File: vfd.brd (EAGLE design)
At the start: 41 parts, among them J1 KEYPAD, J3 ARDUINO_R3, U1 20070-1A04PTH, X1 DRV

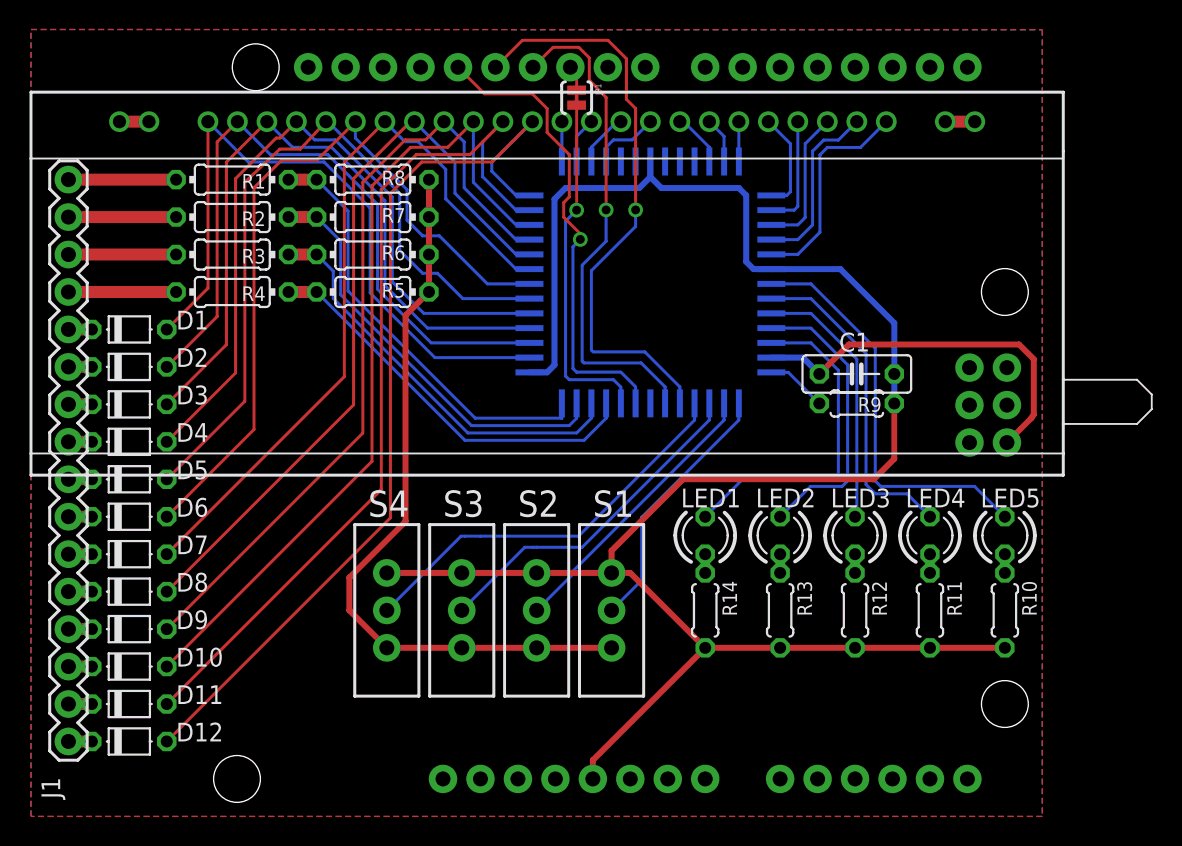
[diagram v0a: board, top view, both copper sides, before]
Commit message: add filament driver components
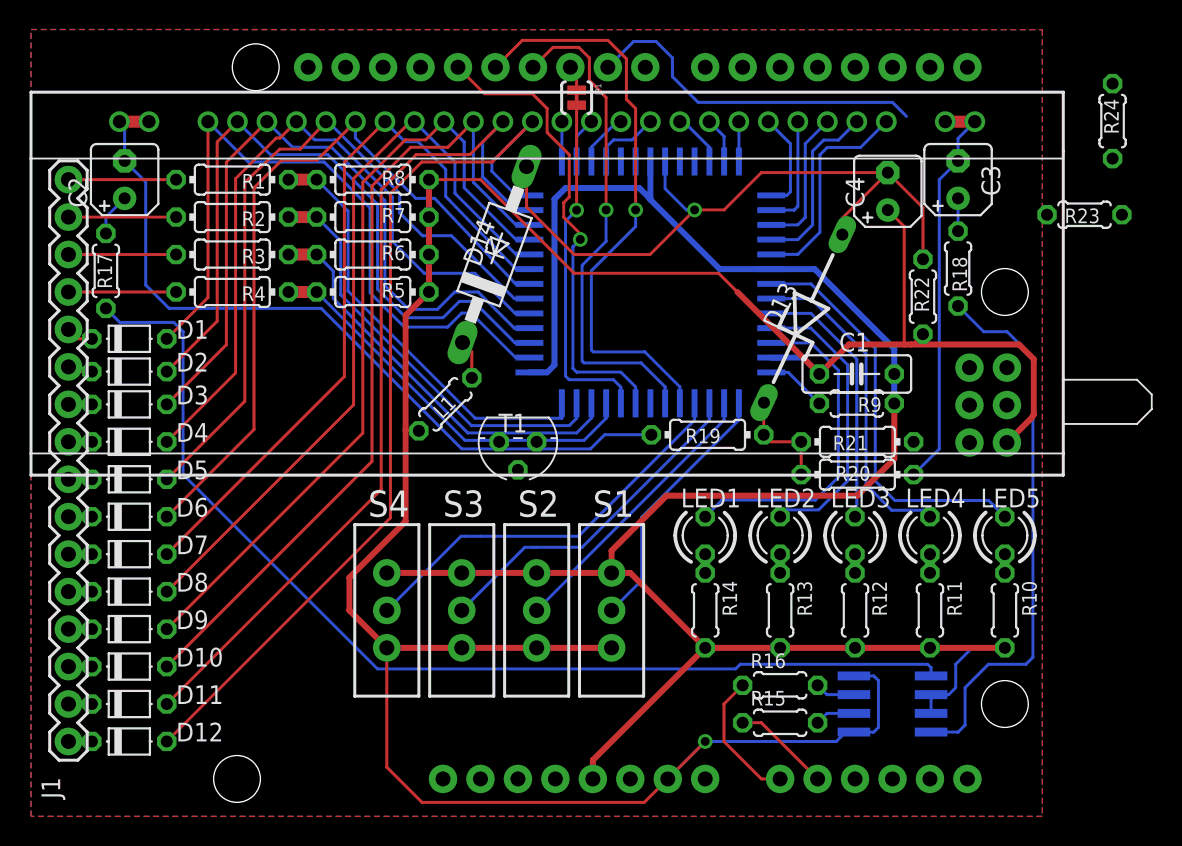
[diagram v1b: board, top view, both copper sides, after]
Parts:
- added C2, C3: 4u7, resistor:B45181A
- added C4: 22uf/50v, resistor:B45181A
- added D13: (no value), diode:ZDIO12.5
- added D14: SS14, diode:F126Z12
- added L1: 1MH, resistor:0204/5
- added R15, R16: 20K, resistor:0204/5
- added R17, R18: 1R0, resistor:0204/5
- added R19, R20: 3k0, resistor:0204/7
- added R21: 100k, resistor:0204/7
- added R22: 100k, resistor:0204/5
- added R23: 10k, resistor:0204/5
- added R24: 1k5, resistor:0204/5
- added T1: 8550, transistor:TO92
- added U$1: L9110, Drivers:SOP8-1.27-5X3.6MM
- moved D1 0.64 mm to (6.67, 32.4)
- moved D2 0.32 mm to (6.67, 30.2)
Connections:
- removed net N$14: X1.P$34
- removed net N$19: J3.AREF
- new net DRVF1: J3.A1, R15.1
- new net DRVF2: J3.A0, R16.1
- new net HVDRV: J3.D9, R24.2
- new net N$26: R15.2, U$1.6
- new net N$27: R16.2, U$1.7
- new net N$28: R17.1, U$1.1
- new net N$29: R18.1, U$1.4
- new net N$30: C2.+, R17.2
- new net N$31: C3.+, R18.2
- new net N$35: D13.C, R19.1, R20.2, R21.2
- new net N$36: R23.1, R24.1, T1.2
- new net N$40: D14.C, L1.1, T1.3
- new net VEE: C4.-, D13.A, D14.A, R22.2, X1.P$34
- net FIL1: now also C2.-, R19.2
- net FIL2: now also C3.-, R20.1
- net GND: now also C4.+, L1.2, R21.1, R22.1, U$1.5, U$1.8
- net VCC: now also R23.2, T1.1, U$1.2, U$1.3
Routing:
- net GND: track 76.2 -> 172.8 mm, vias 0 -> 1
- net N$28: track 0.00 -> 72.5 mm
- net FIL1: track 2.00 -> 53.1 mm
- net VEE: track 0.00 -> 47.7 mm, vias 0 -> 1
- net N$29: track 0.00 -> 37.3 mm
- net FIL2: track 2.00 -> 27.7 mm
- net HVDRV: track 0.00 -> 23.8 mm
- net DRVF2: track 0.00 -> 9.20 mm
- net N$35: track 0.00 -> 7.15 mm
- net DRVF1: track 0.00 -> 6.66 mm
- net VCC: track 133.1 -> 138.7 mm
- net N$30: track 0.00 -> 2.91 mm
- net N$26: track 0.00 -> 2.73 mm
- net N$27: track 0.00 -> 2.73 mm
- net N$40: track 0.00 -> 2.66 mm
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
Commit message: all lines laid
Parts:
- D13: device diode:ZDIO12.5 -> diode:DO34Z7
- D14: device diode:F126Z12 -> diode:DO35-7
- R5, R6, R7, R8: device resistor:0204/7 -> resistor:0204/5
- moved R23 54.9 mm to (21.0, 19.0), turned to 270 degrees
- moved R24 52.2 mm to (28.1, 21.1), turned to 0 degrees
- moved C4 32.4 mm to (29.8, 26.6), turned to 0 degrees
- moved R22 29.4 mm to (34.8, 21.1), turned to 0 degrees
- moved D14 15.0 mm to (32.5, 23.2), turned to 0 degrees
- moved D13 14.3 mm to (42.9, 23.2), turned to 180 degrees
- moved T1 12.0 mm to (21.0, 26.0)
- moved JP1 5.47 mm to (41.0, 45.0)
- moved R8 3.75 mm to (21.0, 40.2)
- moved R7 3.50 mm to (21.0, 37.9)
- moved R6 3.26 mm to (21.0, 35.7)
- moved R1 3.05 mm to (13.2, 40.2)
- moved R5 3.03 mm to (21.0, 33.5)
- moved R2 2.74 mm to (13.2, 37.9)
- moved R3 2.43 mm to (13.2, 35.7)
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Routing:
- net HVDRV: track 23.8 -> 44.4 mm
- net N$28: track 72.5 -> 88.4 mm
- net VCC: track 138.7 -> 151.9 mm
- net GND: track 172.8 -> 160.4 mm, vias 1 -> 0
- net K1: track 27.3 -> 39.0 mm
- net VEE: track 47.7 -> 36.0 mm
- net MISO: track 39.6 -> 29.4 mm
- net N$40: track 2.66 -> 10.9 mm
- net K2: track 28.1 -> 36.2 mm
- net N$36: track 0.00 -> 7.28 mm
- net SS: track 23.8 -> 16.9 mm
- net MOSI: track 33.8 -> 27.6 mm
- net N$18: track 1.73 -> 7.93 mm
- net K3: track 28.7 -> 33.3 mm
- net SEGE: track 56.1 -> 60.4 mm
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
